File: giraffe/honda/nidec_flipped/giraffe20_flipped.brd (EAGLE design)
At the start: 100.3 x 31.8 mm, 6 parts, among them J3 OBDII-FEMALE-CUT, J4 VERT_RJ45, SW1 4XDPSTSMT

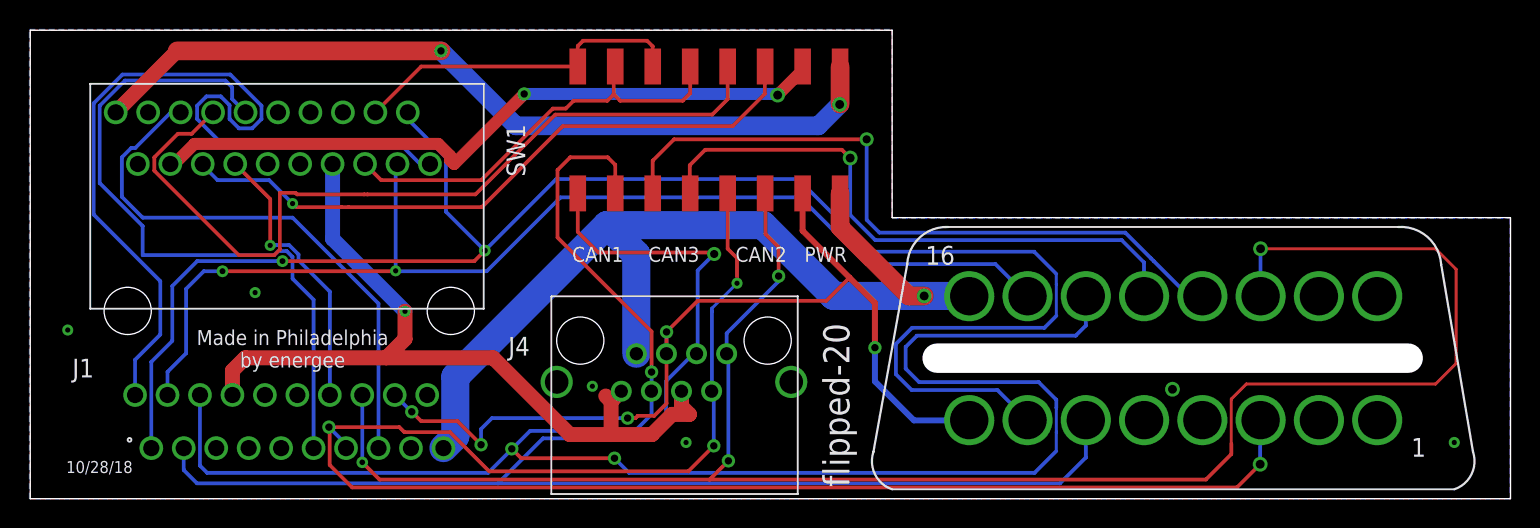
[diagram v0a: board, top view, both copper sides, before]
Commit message: Moved silkscreens
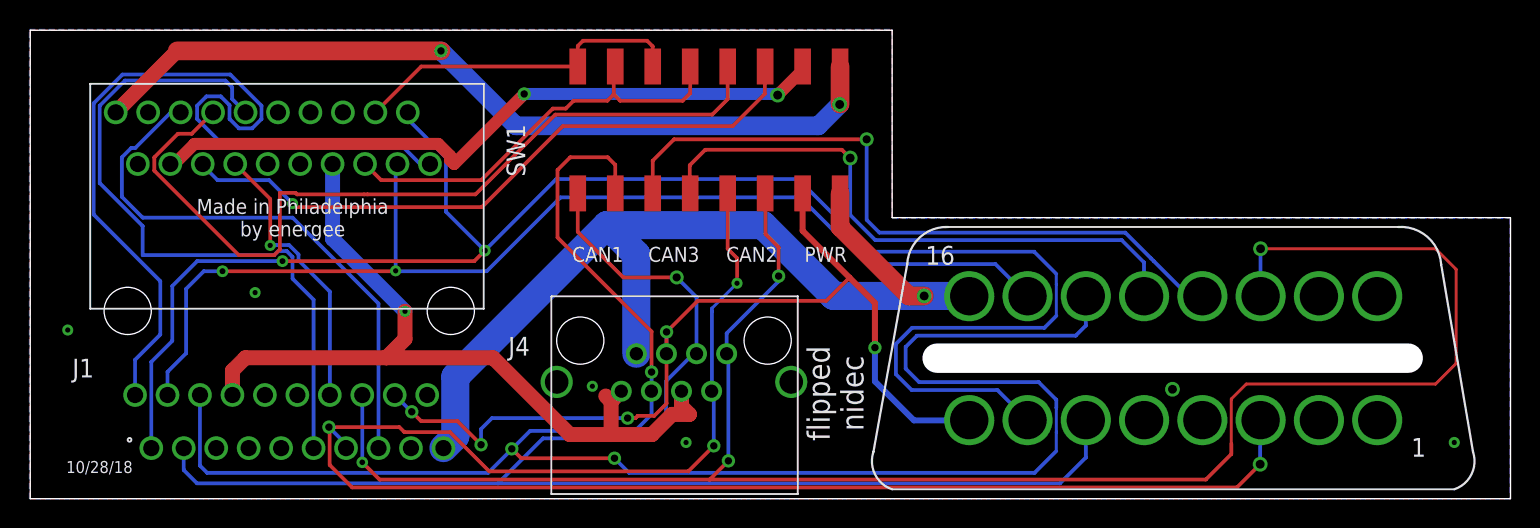
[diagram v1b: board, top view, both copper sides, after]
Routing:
- net CAN1_H: track 104.5 -> 101.2 mm
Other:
- board text added: "flipped nidec"
- board text removed: "flipped-20"
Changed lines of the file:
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@@
 <layers>
 <layer number="1" name="Top" color="4" fill="1" visible="yes" active="yes"/>
-<layer number="2" name="Route2" color="1" fill="3" visible="no" active="yes"/>
+<layer number="2" name="Route2" color="1" fill="3" visible="yes" active="yes"/>
 <layer number="3" name="Route3" color="4" fill="3" visible="no" active="no"/>
 <layer number="4" name="Route4" color="1" fill="4" visible="no" active="no"/>
@@
 <layer number="13" name="Route13" color="4" fill="5" visible="no" active="no"/>
 <layer number="14" name="Route14" color="1" fill="6" visible="no" active="no"/>
-<layer number="15" name="Route15" color="4" fill="6" visible="no" active="yes"/>
+<layer number="15" name="Route15" color="4" fill="6" visible="yes" active="yes"/>
 <layer number="16" name="Bottom" color="1" fill="1" visible="yes" active="yes"/>
 <layer number="17" name="Pads" color="2" fill="1" visible="yes" active="yes"/>
@@
 <vertex x="46.7868" y="0.635"/>
 </polygon>
-<text x="55.5244" y="0.7874" size="1.778" layer="21" font="vector" ratio="10" rot="R90">flipped-20</text>
-<text x="36.7284" y="16.0528" size="1.016" layer="21">CAN1</text>
-<text x="41.8846" y="16.0528" size="1.016" layer="21">CAN3</text>
-<text x="47.8028" y="16.0528" size="1.016" layer="21">CAN2</text>
-<text x="52.4764" y="16.0528" size="1.016" layer="21">PWR</text>
+<text x="54.5719" y="7.1374" size="1.524" layer="21" font="vector" ratio="10" rot="R90" align="center">flipped
+nidec</text>
+<text x="36.7284" y="16.0528" size="1.016" layer="21" font="vector">CAN1</text>
+<text x="41.8846" y="16.0528" size="1.016" layer="21" font="vector">CAN3</text>
+<text x="47.1678" y="16.0528" size="1.016" layer="21" font="vector">CAN2</text>
+<text x="52.4764" y="16.0528" size="1.016" layer="21" font="vector">PWR</text>
 <wire x1="40.8686" y1="17.4244" x2="40.8686" y2="15.5956" width="0.254" layer="51"/>
-<wire x1="47.244" y1="17.5006" x2="47.244" y2="15.6718" width="0.254" layer="51"/>
+<wire x1="46.2915" y1="17.5006" x2="46.2915" y2="15.6718" width="0.254" layer="51"/>
 <wire x1="51.6382" y1="17.5768" x2="51.6382" y2="15.748" width="0.254" layer="51"/>
 <wire x1="55.8546" y1="17.5006" x2="55.8546" y2="15.6718" width="0.254" layer="51"/>
@@
 <text x="4.6863" y="2.1463" size="0.8128" layer="21" font="vector" rot="R180" align="center">10/28/18</text>
 <wire x1="61.468" y1="9.525" x2="93.3958" y2="9.525" width="1.99898125" layer="20"/>
-<text x="17.78" y="10.16" size="1.016" layer="21" font="vector" align="center">Made in Philadelphia
+<text x="17.78" y="19.05" size="1.016" layer="21" font="vector" align="center">Made in Philadelphia
 by energee</text>
 </plain>
@@
 <contactref element="J4" pad="6"/>
 <contactref element="SW1" pad="1"/>
-<via x="46.355" y="16.5862" extent="1-16" drill="0.55"/>
+<via x="43.815" y="14.9987" extent="1-16" drill="0.55"/>
 <wire x1="71.5518" y1="2.794" x2="69.7992" y2="1.0414" width="0.254" layer="16"/>
 <wire x1="31.706509375" y1="1.0414" x2="11.303" y2="1.0414" width="0.254" layer="16"/>
 <wire x1="31.706509375" y1="1.0414" x2="69.7992" y2="1.0414" width="0.254" layer="16"/>
 <wire x1="37.11" y1="20.6936" x2="37.11" y2="18.0842" width="0.254" layer="1"/>
-<wire x1="37.11" y1="18.0842" x2="38.5064" y2="16.6878" width="0.254" layer="1"/>
-<wire x1="38.5064" y1="16.6878" x2="46.2534" y2="16.6878" width="0.254" layer="1"/>
-<wire x1="46.2534" y1="16.6878" x2="46.355" y2="16.5862" width="0.254" layer="1"/>
 <wire x1="44.9532" y1="9.825" x2="45.16" y2="9.825" width="0.254" layer="16"/>
 <wire x1="43.0906" y1="7.9624" x2="44.9532" y2="9.825" width="0.254" layer="16"/>
 <wire x1="45.16" y1="9.825" x2="45.2374" y2="9.9024" width="0.254" layer="16"/>
-<wire x1="45.2374" y1="15.4686" x2="45.2374" y2="9.9024" width="0.254" layer="16"/>
 <wire x1="43.0906" y1="5.5494" x2="43.0906" y2="7.9624" width="0.254" layer="16"/>
 <wire x1="34.754509375" y1="4.0894" x2="41.6306" y2="4.0894" width="0.254" layer="16"/>
 <wire x1="41.6306" y1="4.0894" x2="43.0906" y2="5.5494" width="0.254" layer="16"/>
 <wire x1="34.754509375" y1="4.0894" x2="31.706509375" y2="1.0414" width="0.254" layer="16"/>
-<wire x1="46.355" y1="16.5862" x2="45.2374" y2="15.4686" width="0.254" layer="16"/>
 <wire x1="71.545" y1="5.325" x2="71.545" y2="2.8008" width="0.254" layer="16"/>
 <wire x1="71.545" y1="2.8008" x2="71.5518" y2="2.794" width="0.254" layer="16"/>
+<wire x1="43.815" y1="14.9987" x2="40.1955" y2="14.9987" width="0.254" layer="1"/>
+<wire x1="40.1955" y1="14.9987" x2="37.11" y2="18.0842" width="0.254" layer="1"/>
+<wire x1="45.16" y1="9.825" x2="45.16" y2="13.6537" width="0.254" layer="16"/>
+<wire x1="45.16" y1="13.6537" x2="43.815" y2="14.9987" width="0.254" layer="16"/>
 </signal>
 <signal name="K_LIN">

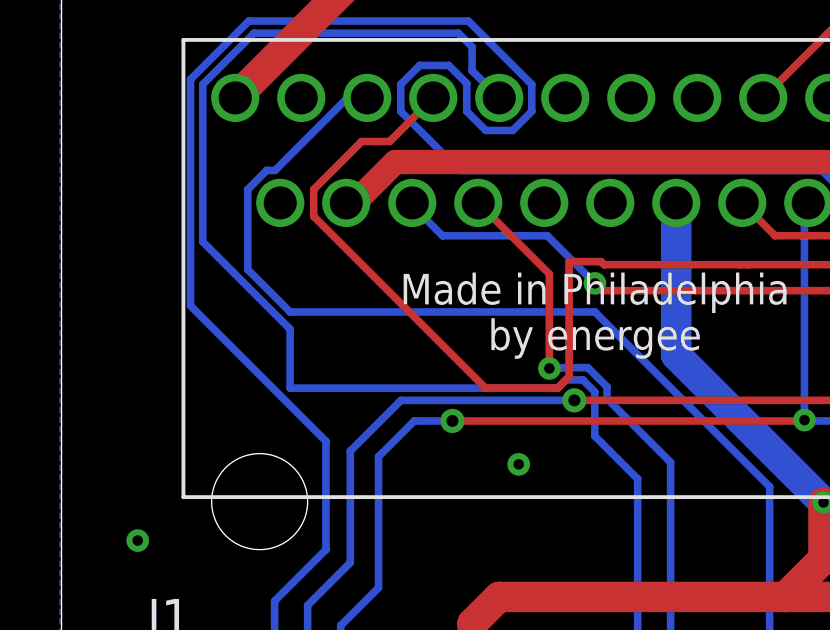
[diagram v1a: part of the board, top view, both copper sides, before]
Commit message: Fixed ground vias
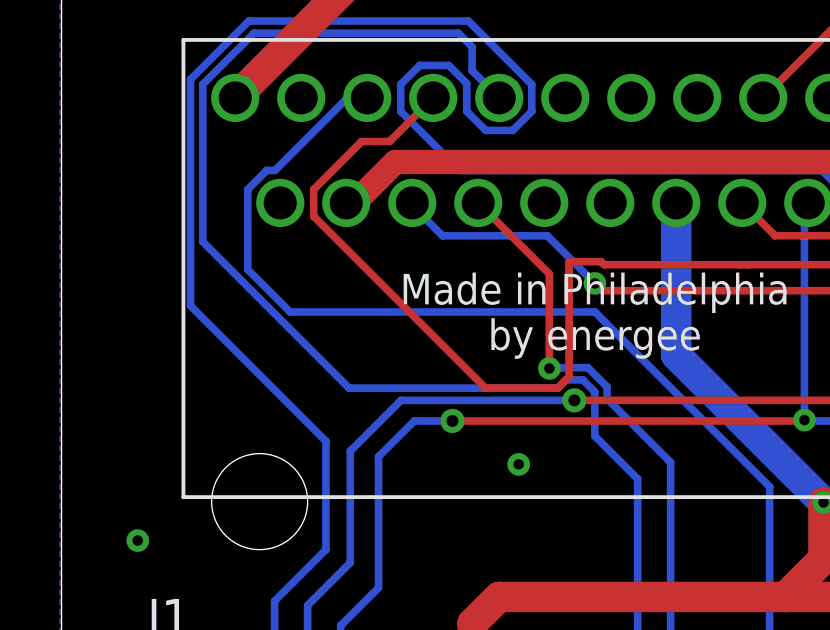
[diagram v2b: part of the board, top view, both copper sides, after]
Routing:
- net MDX_CANH: track 47.3 -> 46.1 mm
- net GND: vias 2 -> 7
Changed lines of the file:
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@@
 <wire x1="25.4" y1="10.8204" x2="25.4" y2="12.7" width="1.016" layer="1"/>
 <wire x1="25.4" y1="12.7" x2="20.491" y2="17.609" width="1.016" layer="16"/>
+<via x="2.54" y="11.43" extent="1-16" drill="0.35"/>
+<via x="38.1" y="7.62" extent="1-16" drill="0.35"/>
+<via x="96.52" y="3.81" extent="1-16" drill="0.35"/>
+<via x="15.24" y="13.97" extent="1-16" drill="0.35"/>
+<via x="44.45" y="3.81" extent="1-16" drill="0.35"/>
+<wire x1="44.6786" y1="5.715" x2="44.45" y2="3.81" width="0" layer="19" extent="1-1"/>
 </signal>
 <signal name="CAN1_L">
@@
 <wire x1="19.204" y1="13.4858" x2="17.7768" y2="14.913" width="0.254" layer="16"/>
 <wire x1="17.7768" y1="14.913" x2="17.7768" y2="16.38634375" width="0.254" layer="16"/>
-<wire x1="16.53525625" y1="16.51" x2="7.62" y2="16.51" width="0.254" layer="16"/>
-<wire x1="7.62" y1="16.51" x2="7.62" y2="18.4752625" width="0.254" layer="16"/>
-<wire x1="7.62" y1="18.4752625" x2="4.7076" y2="21.3876625" width="0.254" layer="16"/>
 <wire x1="4.7076" y1="21.3876625" x2="4.7076" y2="26.6335625" width="0.254" layer="16"/>
 <wire x1="13.22736875" y1="28.3416" x2="13.6858" y2="27.88316875" width="0.254" layer="16"/>
@@
 <wire x1="4.7076" y1="26.6335625" x2="6.4156375" y2="28.3416" width="0.254" layer="16"/>
 <wire x1="13.6858" y1="27.09" x2="14.591" y2="26.1848" width="0.254" layer="16"/>
+<wire x1="16.53525625" y1="16.51" x2="9.5852625" y2="16.51" width="0.254" layer="16"/>
+<wire x1="9.5852625" y1="16.51" x2="4.7076" y2="21.3876625" width="0.254" layer="16"/>
 </signal>
 <signal name="MDX_CANL">
@@
 <wire x1="18.1832" y1="16.55468125" x2="17.54528125" y2="17.1926" width="0.254" layer="16"/>
 </signal>
-<signal name="N$1">
-<via x="38.1" y="7.62" extent="1-16" drill="0.35"/>
-</signal>
-<signal name="N$2">
-<via x="44.45" y="3.81" extent="1-16" drill="0.35"/>
-</signal>
-<signal name="N$4">
-<via x="15.24" y="13.97" extent="1-16" drill="0.35"/>
-</signal>
-<signal name="N$5">
-<via x="2.54" y="11.43" extent="1-16" drill="0.35"/>
-</signal>
-<signal name="N$6">
-<via x="96.52" y="3.81" extent="1-16" drill="0.35"/>
-</signal>
 </signals>

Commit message: Updated both board traces
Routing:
- net CAN2_H: track 118.0 -> 87.2 mm, vias 4 -> 3
- net LDW_IND: track 60.6 -> 30.1 mm, vias 0 -> 1
- net CAN2_L: track 129.9 -> 105.3 mm, vias 4 -> 2
- net MDX_CANH: track 46.1 -> 26.2 mm, vias 0 -> 1
- net CAN1_L: track 131.9 -> 117.6 mm, vias 3 -> 2
- net CAN2_H': track 56.3 -> 45.4 mm
- net IGN: track 64.1 -> 53.9 mm, vias 5 -> 2
- net CAN1_H: track 101.2 -> 92.3 mm, vias 1 -> 2
- net K_LIN: track 115.5 -> 113.0 mm
- net CAN3_L: track 40.9 -> 38.8 mm
- net GND: track 56.9 -> 55.2 mm, vias 7 -> 9
- net CAN3_H: track 47.7 -> 46.1 mm
- net IGN': track 47.1 -> 45.9 mm, vias 2 -> 3
- net L_LIN: track 77.4 -> 76.3 mm
- net MDX_CANL: track 19.1 -> 18.3 mm
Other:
- board text added: "10/30/18"
- board text removed: "10/28/18"
